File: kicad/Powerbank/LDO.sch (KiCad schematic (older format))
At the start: 1 part

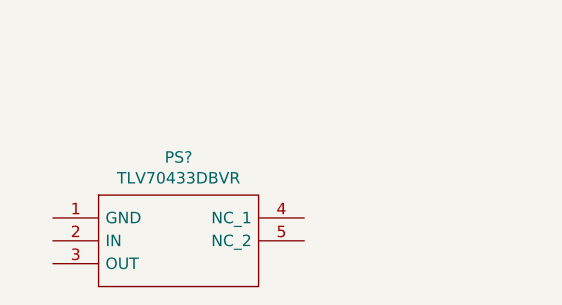
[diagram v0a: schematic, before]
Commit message: Completed buck according to reference guide
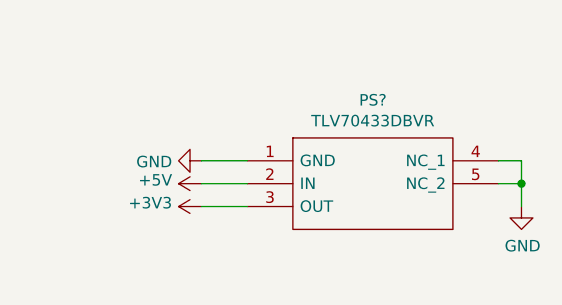
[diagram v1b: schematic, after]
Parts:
- removed PS?: TLV70433DBVR, SOT95P280X145-5N, symbol Powerbank:TLV70433DBVR
- added PS?: TLV70433DBVR, SOT95P280X145-5N, symbol Powerbank:TLV70433DBVR
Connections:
- new net +3V3: PS?.3 (OUT)
- new net +5V: PS?.2 (IN)
- new net GND: PS?.1 (GND), PS?.4 (NC_1), PS?.5 (NC_2)
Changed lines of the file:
@@
 $Comp
 L Powerbank:TLV70433DBVR PS?
-U 1 1 5E0D1B80
-P 5100 3750
-F 0 "PS?" H 5650 4015 50  0000 C CNN
-F 1 "TLV70433DBVR" H 5650 3924 50  0000 C CNN
-F 2 "SOT95P280X145-5N" H 6050 3850 50  0001 L CNN
-F 3 "http://www.ti.com/lit/gpn/tlv704" H 6050 3750 50  0001 L CNN
-F 4 "24V Input Voltage, 150mA, Ultra-Low-Iq Low-Dropout (LDO) Regulators" H 6050 3650 50  0001 L CNN "Description"
-F 5 "1.45" H 6050 3550 50  0001 L CNN "Height"
-F 6 "595-TLV70433DBVR" H 6050 3450 50  0001 L CNN "Mouser Part Number"
-F 7 "https://www.mouser.com/Search/Refine.aspx?Keyword=595-TLV70433DBVR" H 6050 3350 50  0001 L CNN "Mouser Price/Stock"
-F 8 "Texas Instruments" H 6050 3250 50  0001 L CNN "Manufacturer_Name"
-F 9 "TLV70433DBVR" H 6050 3150 50  0001 L CNN "Manufacturer_Part_Number"
-	1    5100 3750
+U 1 1 5E72EB88
+P 5950 3500
+F 0 "PS?" H 6500 3765 50  0000 C CNN
+F 1 "TLV70433DBVR" H 6500 3674 50  0000 C CNN
+F 2 "SOT95P280X145-5N" H 6900 3600 50  0001 L CNN
+F 3 "http://www.ti.com/lit/gpn/tlv704" H 6900 3500 50  0001 L CNN
+F 4 "24V Input Voltage, 150mA, Ultra-Low-Iq Low-Dropout (LDO) Regulators" H 6900 3400 50  0001 L CNN "Description"
+F 5 "1.45" H 6900 3300 50  0001 L CNN "Height"
+F 6 "595-TLV70433DBVR" H 6900 3200 50  0001 L CNN "Mouser Part Number"
+F 7 "https://www.mouser.com/Search/Refine.aspx?Keyword=595-TLV70433DBVR" H 6900 3100 50  0001 L CNN "Mouser Price/Stock"
+F 8 "Texas Instruments" H 6900 3000 50  0001 L CNN "Manufacturer_Name"
+F 9 "TLV70433DBVR" H 6900 2900 50  0001 L CNN "Manufacturer_Part_Number"
+	1    5950 3500
 	1    0    0    -1
 $EndComp
+$Comp
+L power:GND #PWR?
+U 1 1 5E72EB8E
+P 5750 3500
+F 0 "#PWR?" H 5750 3250 50  0001 C CNN
+F 1 "GND" V 5755 3372 50  0000 R CNN
+F 2 "" H 5750 3500 50  0001 C CNN
+F 3 "" H 5750 3500 50  0001 C CNN
+	1    5750 3500
+	0    1    1    0
+$EndComp
+Wire Wire Line
+	5950 3500 5750 3500
+Wire Wire Line
+	7050 3500 7150 3500
+Wire Wire Line
+	7150 3500 7150 3600
+Wire Wire Line
+	7150 3600 7050 3600
+Wire Wire Line
+	7150 3600 7150 3700
+Connection ~ 7150 3600
+$Comp
+L power:GND #PWR?
+U 1 1 5E72EB9B
+P 7150 3700
+F 0 "#PWR?" H 7150 3450 50  0001 C CNN
+F 1 "GND" H 7155 3527 50  0000 C CNN
+F 2 "" H 7150 3700 50  0001 C CNN
+F 3 "" H 7150 3700 50  0001 C CNN
+	1    7150 3700
+	1    0    0    -1
+$EndComp
+$Comp
+L power:+3V3 #PWR?
+U 1 1 5E72EBA1
+P 5750 3700
+F 0 "#PWR?" H 5750 3550 50  0001 C CNN
+F 1 "+3V3" V 5765 3828 50  0000 L CNN
+F 2 "" H 5750 3700 50  0001 C CNN
+F 3 "" H 5750 3700 50  0001 C CNN
+	1    5750 3700
+	0    -1   -1   0
+$EndComp
+Wire Wire Line
+	5750 3700 5950 3700
+$Comp
+L power:+5V #PWR?
+U 1 1 5E72EE4D
+P 5750 3600
+F 0 "#PWR?" H 5750 3450 50  0001 C CNN
+F 1 "+5V" V 5765 3728 50  0000 L CNN
+F 2 "" H 5750 3600 50  0001 C CNN
+F 3 "" H 5750 3600 50  0001 C CNN
+	1    5750 3600
+	0    -1   -1   0
+$EndComp
+Wire Wire Line
+	5750 3600 5950 3600
 $EndSCHEMATC

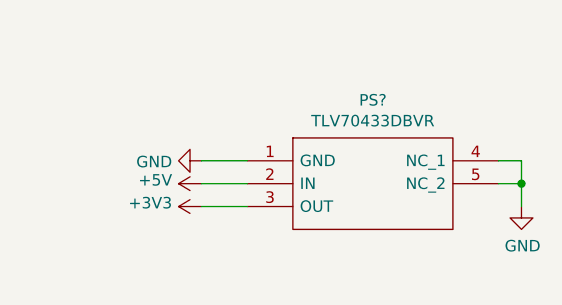
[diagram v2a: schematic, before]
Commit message: Moved LDO to Buck sheet and started check of components
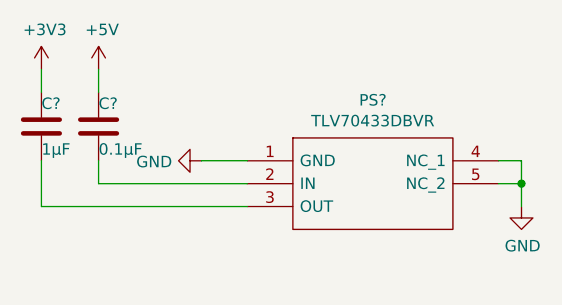
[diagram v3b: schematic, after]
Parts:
- added C?: 0.1µF, symbol Device:C
- added C?: 1µF, symbol Device:C
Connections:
- net +3V3: now also C?.2; no longer PS?.3 (OUT)
- net +5V: now also C?.2; no longer PS?.2 (IN)
- new net: C?.1, PS?.2 (IN)
- new net: C?.1, PS?.3 (OUT)
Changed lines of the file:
@@
 U 1 1 5E72EB8E
 P 5750 3500
+AR Path="/5E0D0913/5E72EB8E" Ref="#PWR?"  Part="1"
+AR Path="/5E0D16A0/5E72EB8E" Ref="#PWR?"  Part="1"
 F 0 "#PWR?" H 5750 3250 50  0001 C CNN
 F 1 "GND" V 5755 3372 50  0000 R CNN
@@
 U 1 1 5E72EB9B
 P 7150 3700
+AR Path="/5E0D0913/5E72EB9B" Ref="#PWR?"  Part="1"
+AR Path="/5E0D16A0/5E72EB9B" Ref="#PWR?"  Part="1"
 F 0 "#PWR?" H 7150 3450 50  0001 C CNN
 F 1 "GND" H 7155 3527 50  0000 C CNN
@@
 L power:+3V3 #PWR?
 U 1 1 5E72EBA1
-P 5750 3700
-F 0 "#PWR?" H 5750 3550 50  0001 C CNN
-F 1 "+3V3" V 5765 3828 50  0000 L CNN
-F 2 "" H 5750 3700 50  0001 C CNN
-F 3 "" H 5750 3700 50  0001 C CNN
-	1    5750 3700
-	0    -1   -1   0
+P 5050 3100
+AR Path="/5E0D0913/5E72EBA1" Ref="#PWR?"  Part="1"
+AR Path="/5E0D16A0/5E72EBA1" Ref="#PWR?"  Part="1"
+F 0 "#PWR?" H 5050 2950 50  0001 C CNN
+F 1 "+3V3" H 5065 3273 50  0000 C CNN
+F 2 "" H 5050 3100 50  0001 C CNN
+F 3 "" H 5050 3100 50  0001 C CNN
+	1    5050 3100
+	1    0    0    -1
 $EndComp
-Wire Wire Line
-	5750 3700 5950 3700
 $Comp
 L power:+5V #PWR?
 U 1 1 5E72EE4D
-P 5750 3600
-F 0 "#PWR?" H 5750 3450 50  0001 C CNN
-F 1 "+5V" V 5765 3728 50  0000 L CNN
-F 2 "" H 5750 3600 50  0001 C CNN
-F 3 "" H 5750 3600 50  0001 C CNN
-	1    5750 3600
-	0    -1   -1   0
+P 5300 3100
+F 0 "#PWR?" H 5300 2950 50  0001 C CNN
+F 1 "+5V" H 5315 3273 50  0000 C CNN
+F 2 "" H 5300 3100 50  0001 C CNN
+F 3 "" H 5300 3100 50  0001 C CNN
+	1    5300 3100
+	1    0    0    -1
+$EndComp
+$Comp
+L Device:C C?
+U 1 1 5EA0DA84
+P 5300 3350
+AR Path="/5E0D0913/5EA0DA84" Ref="C?"  Part="1"
+AR Path="/5E0D16A0/5EA0DA84" Ref="C?"  Part="1"
+F 0 "C?" H 5300 3250 50  0000 R CNN
+F 1 "0.1µF" H 5300 3450 50  0000 R CNN
+F 2 "" H 5338 3200 50  0001 C CNN
+F 3 "~" H 5300 3350 50  0001 C CNN
+	1    5300 3350
+	-1   0    0    1
 $EndComp
 Wire Wire Line
-	5750 3600 5950 3600
+	5300 3100 5300 3200
+Wire Wire Line
+	5300 3500 5300 3600
+Wire Wire Line
+	5300 3600 5950 3600
+$Comp
+L Device:C C?
+U 1 1 5EA0F071
+P 5050 3350
+AR Path="/5E0D0913/5EA0F071" Ref="C?"  Part="1"
+AR Path="/5E0D16A0/5EA0F071" Ref="C?"  Part="1"
+F 0 "C?" H 5050 3250 50  0000 R CNN
+F 1 "1µF" H 5050 3450 50  0000 R CNN
+F 2 "" H 5088 3200 50  0001 C CNN
+F 3 "~" H 5050 3350 50  0001 C CNN
+	1    5050 3350
+	-1   0    0    1
+$EndComp
+Wire Wire Line
+	5050 3200 5050 3100
+Wire Wire Line
+	5050 3500 5050 3700
+Wire Wire Line
+	5050 3700 5950 3700
 $EndSCHEMATC
